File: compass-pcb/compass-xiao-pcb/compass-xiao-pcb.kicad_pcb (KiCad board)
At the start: 2 copper layers, 72.2 x 72 mm, 23 parts

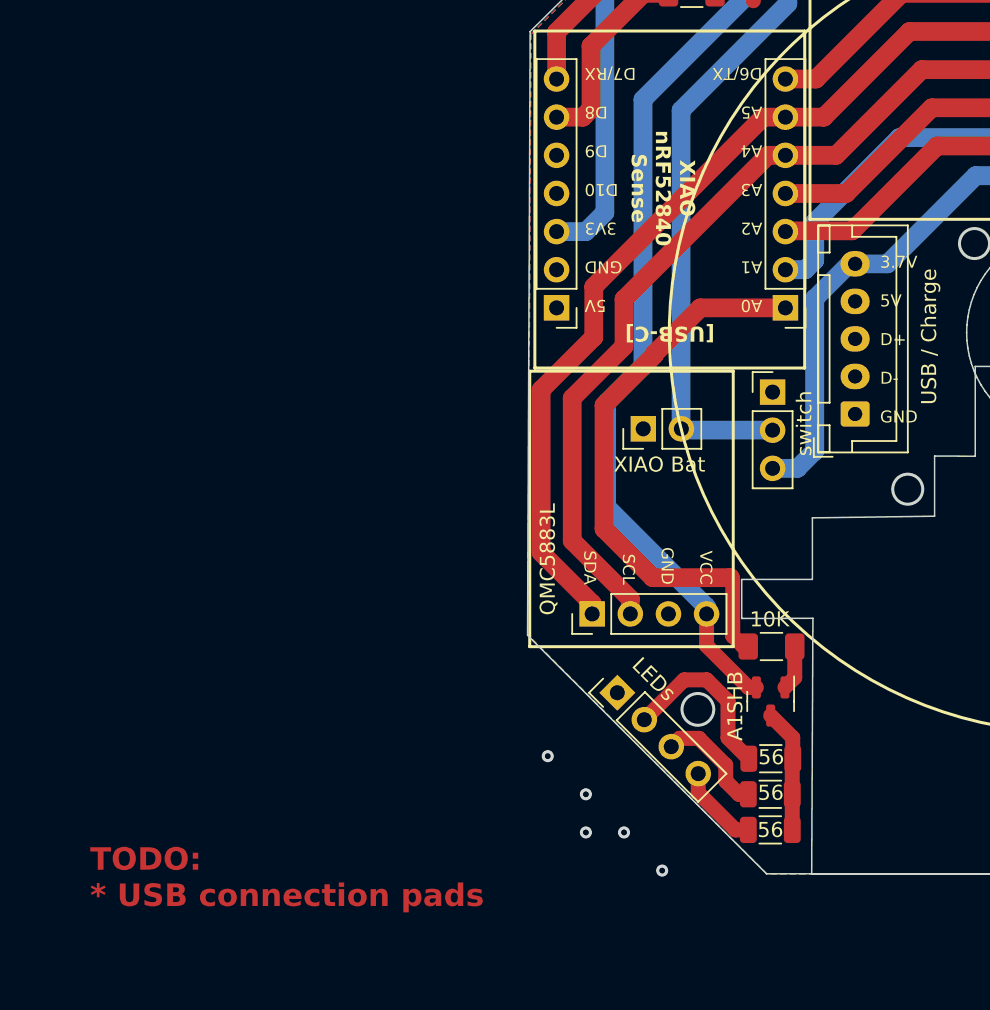
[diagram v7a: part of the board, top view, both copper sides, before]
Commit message: USB pads
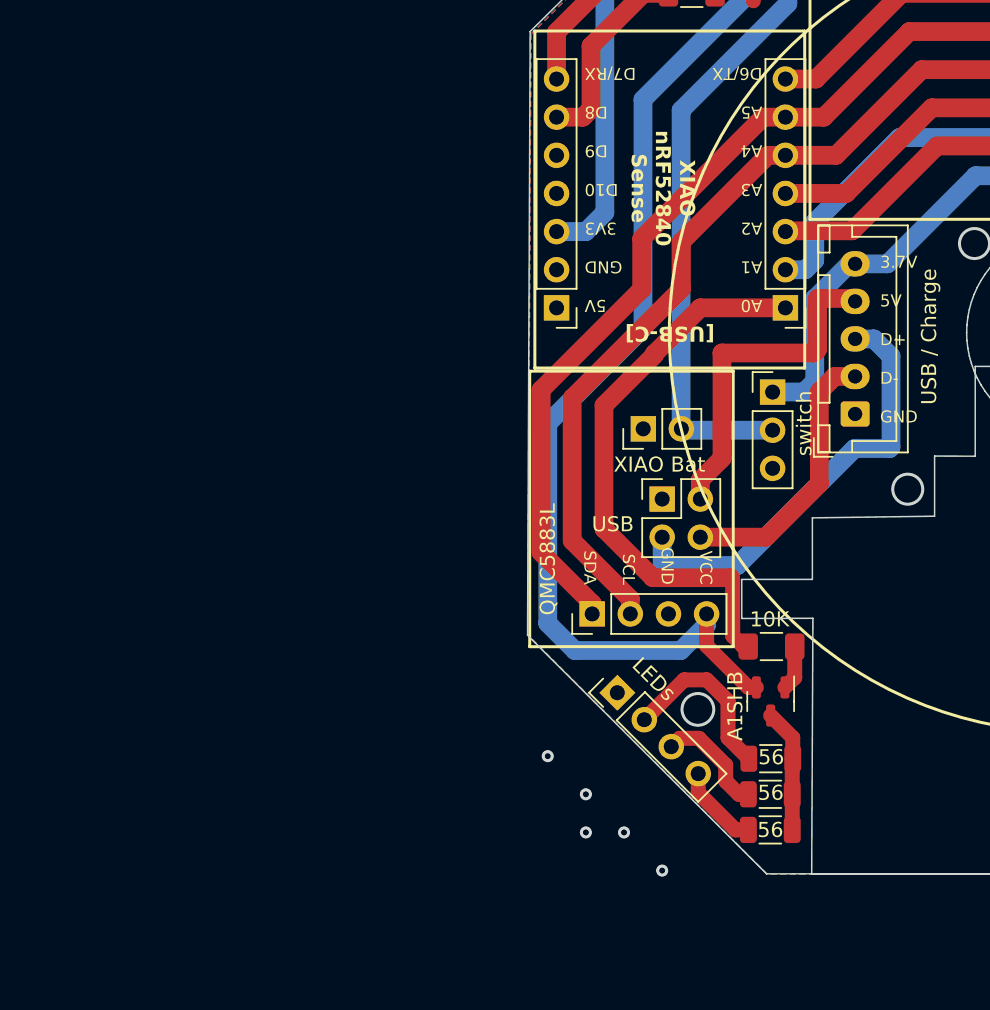
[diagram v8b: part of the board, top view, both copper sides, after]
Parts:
- added USB: PinHeader_2x02_P2.54mm_Vertical, Connector_PinHeader_2.54mm:PinHeader_2x02_P2.54mm_Vertical, F.Cu at (200.7, 87.0)
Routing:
- net (no net): track 1030.8 -> 1108.9 mm
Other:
- board text removed: "TODO: * USB connection pads"
